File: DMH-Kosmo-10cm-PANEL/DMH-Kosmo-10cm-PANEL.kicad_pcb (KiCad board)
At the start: 2 copper layers, 100 x 200 mm, 4 parts

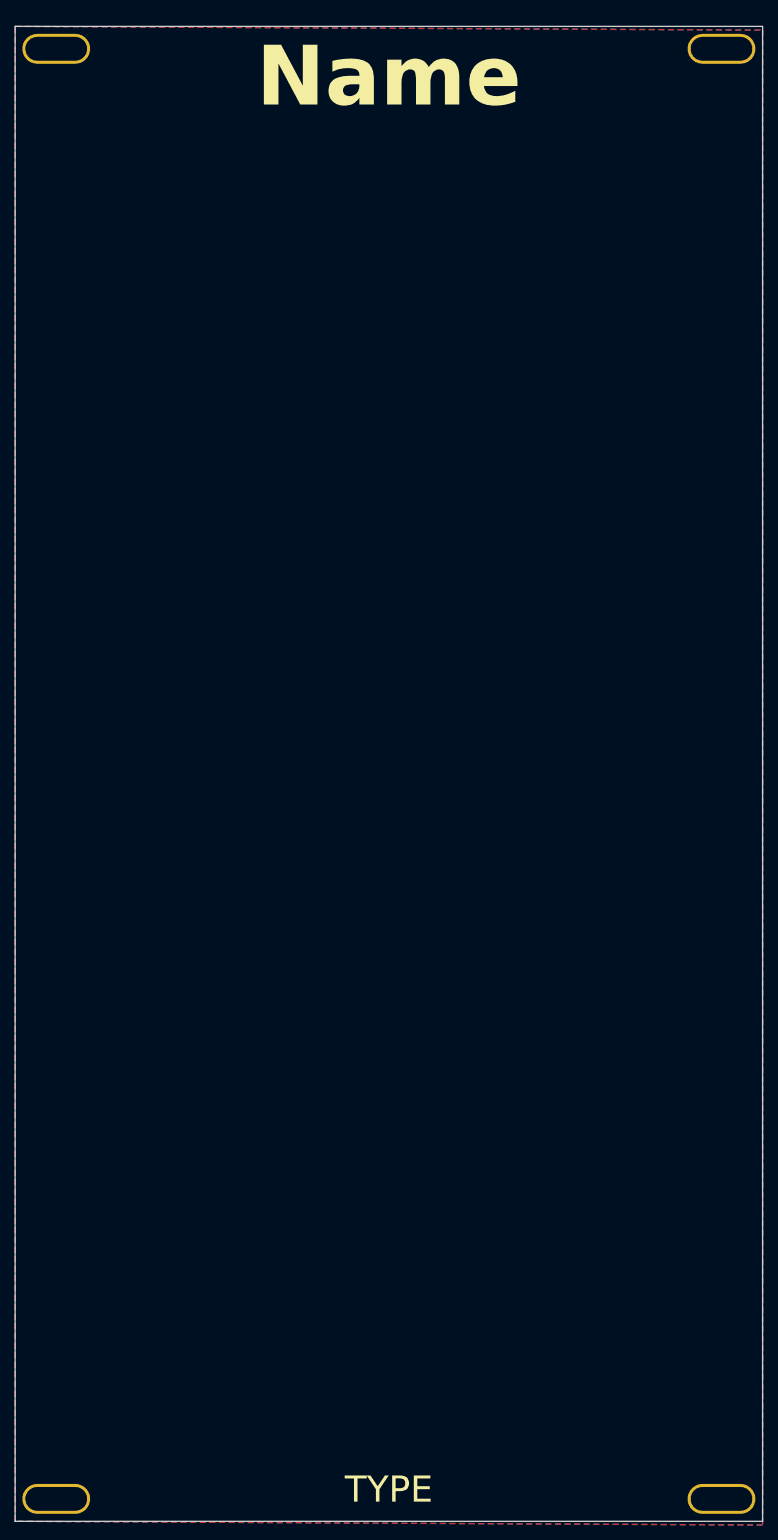
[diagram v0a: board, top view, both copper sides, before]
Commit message: Updated 5cm and 10 templates
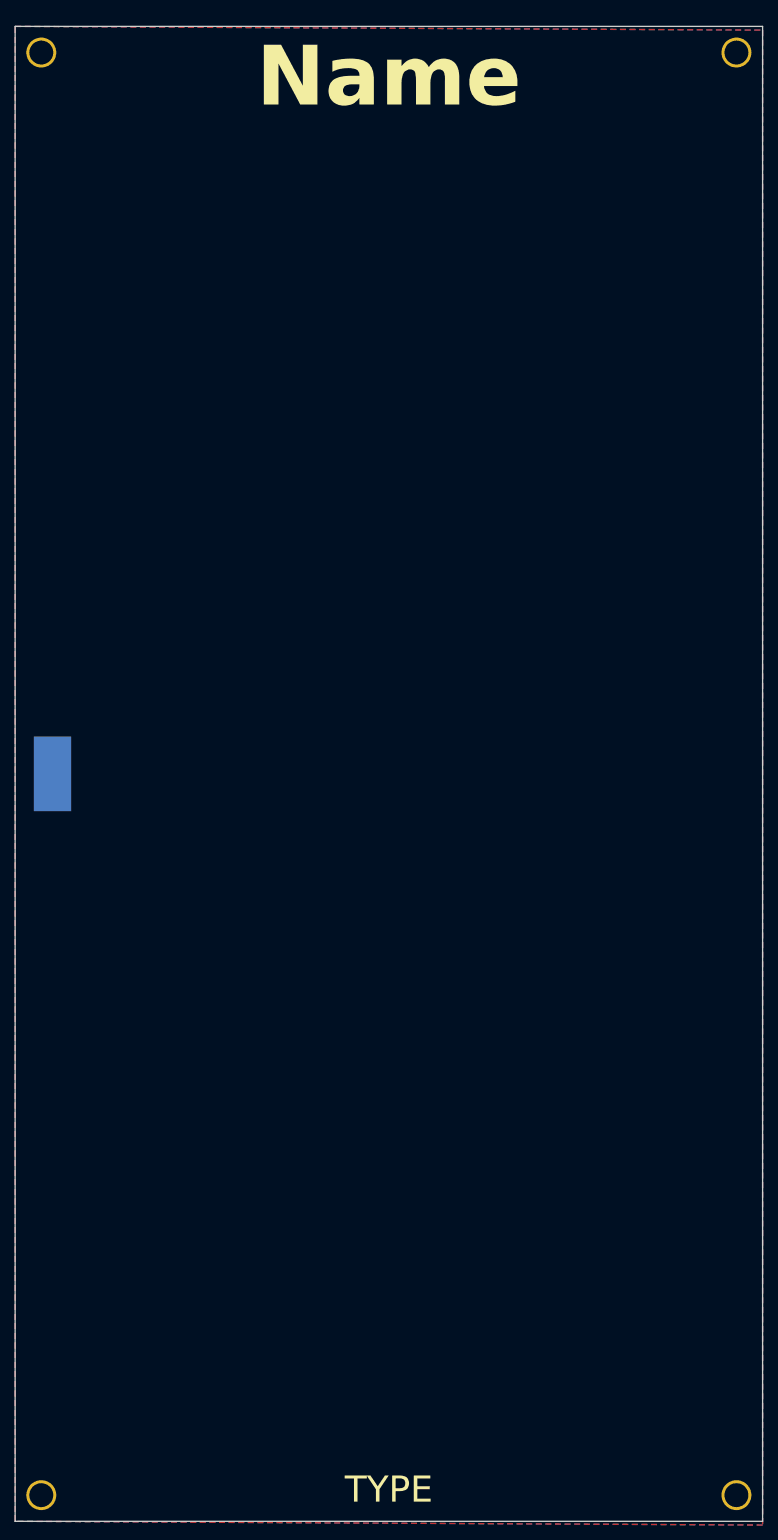
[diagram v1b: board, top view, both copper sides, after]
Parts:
- added J0: Panel_GND_Solder_Wire_Pad, SynthStuff:Panel_GND_SolderWirePad_5x10mm, B.Cu at (55.0, 130.0)
- H1, H2, H3, H4: footprint SynthStuff:MountingHole_Slotted_Rails -> SynthStuff:MountingHole_Rails
- moved H1 2.06 mm to (53.5, 33.5)
- moved H2 2.06 mm to (146.5, 33.5)
- moved H3 2.06 mm to (53.5, 226.5)
- moved H4 2.06 mm to (146.5, 226.5)
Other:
- board text added: "Mk1.0 - Month Year"
- board text removed: "JLCJLCJLCJLC"
